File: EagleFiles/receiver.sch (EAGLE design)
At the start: 9 parts, among them IC1 MEGA8-AI

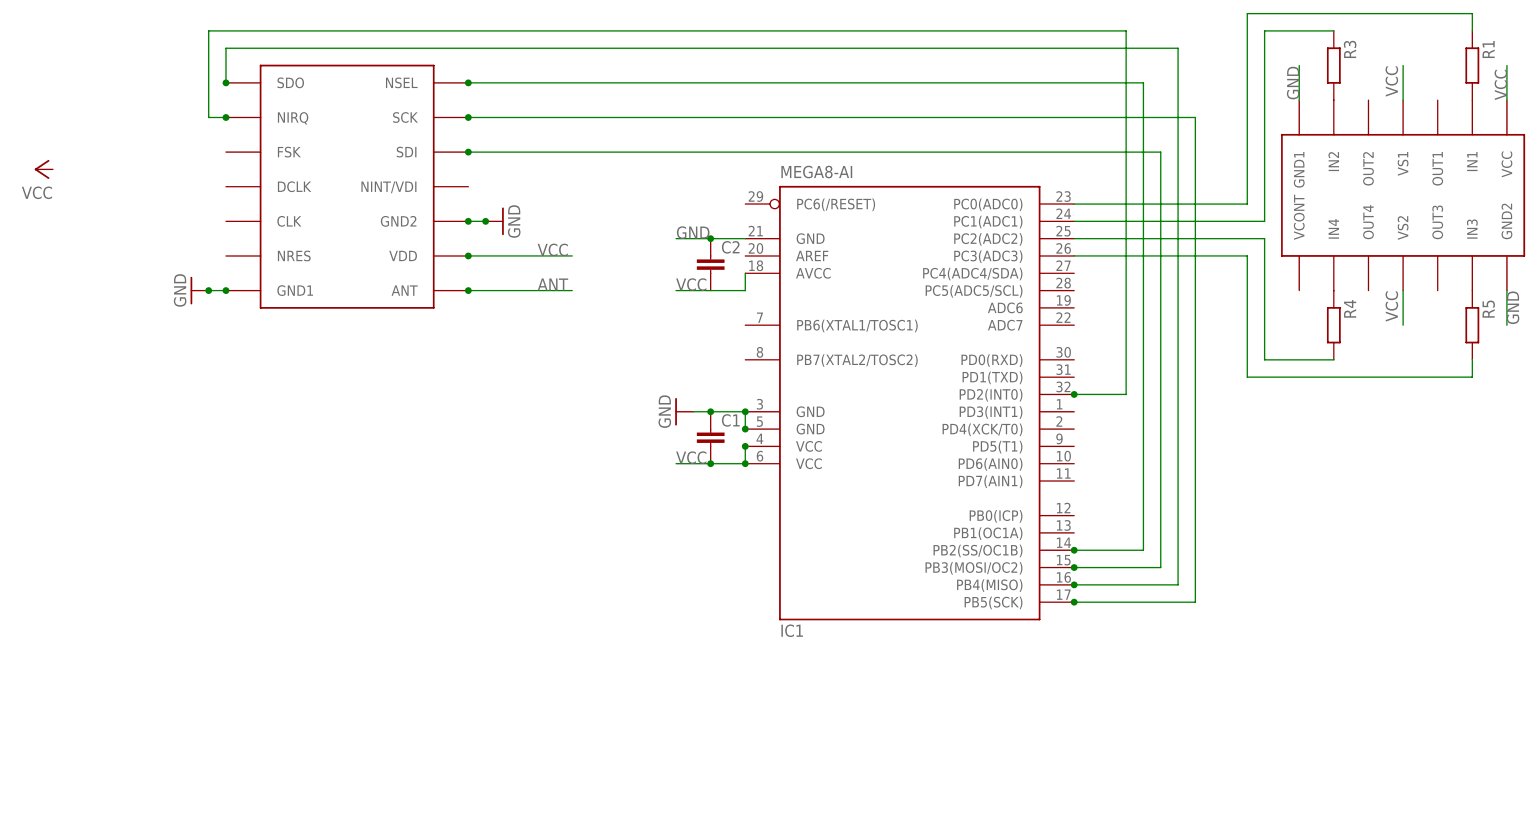
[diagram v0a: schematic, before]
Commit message: Further development of the schematic and board
Schematic finalized, added a pinheader for programming and corrected
wiring errors. Board largely designed, including pads to solder the
motor and servo wires to.
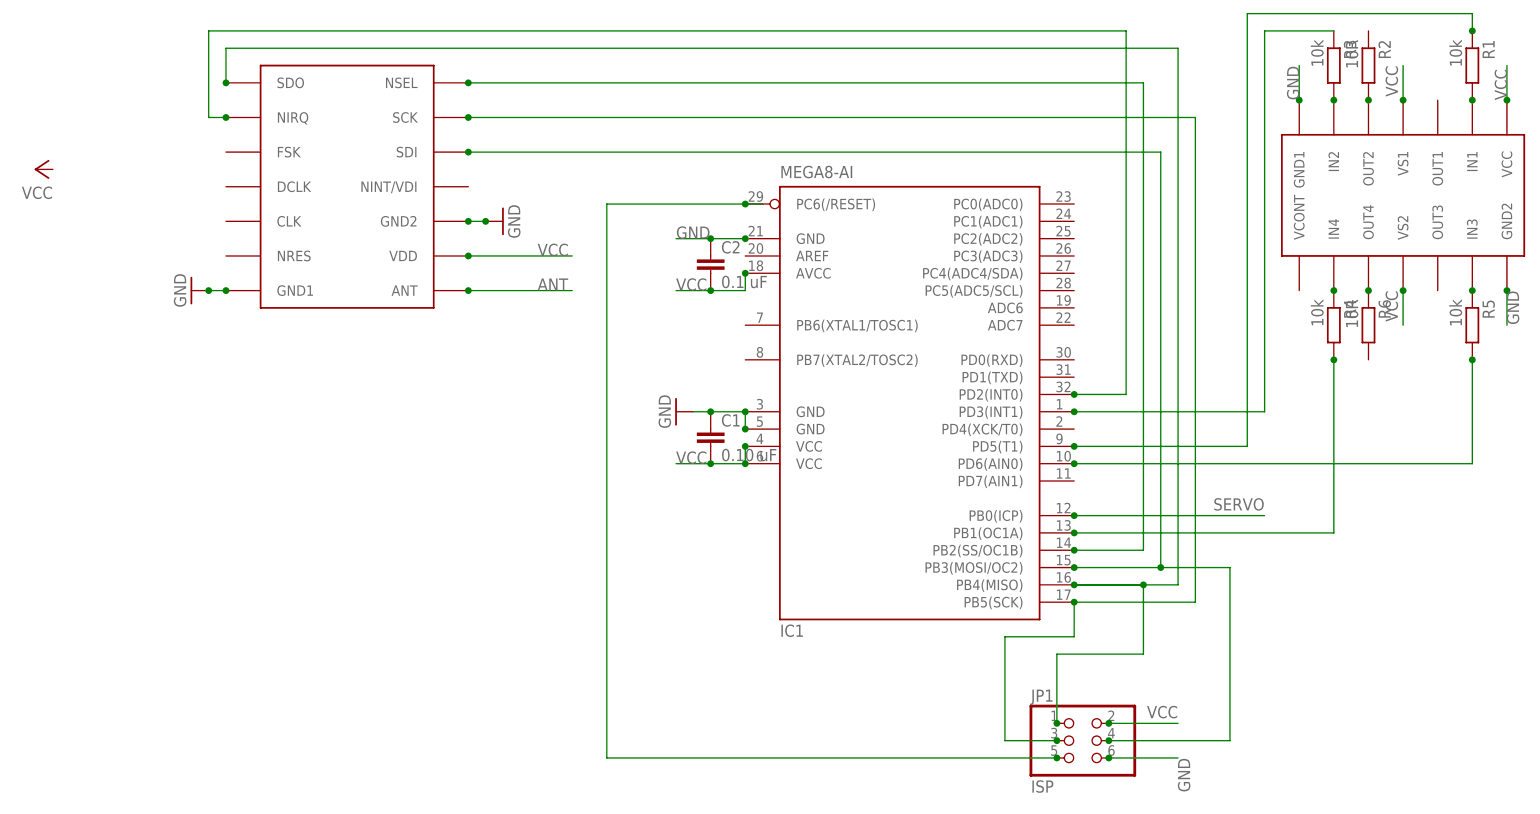
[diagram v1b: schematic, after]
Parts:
- added JP1: ISP, pinhead:PINHD-2X3
- added R2, R6: 10R, resistor:R-EU_R2012
- C1: value (none) -> 0.10 uF
- C2: value (none) -> 0.1 uF
- R1, R3, R4, R5: value (none) -> 10k
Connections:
- new net N$14: LB1836M.OUT2, R2.2
- new net N$15: LB1836M.OUT4, R6.1
- new net N$20: IC1.PC6(/RESET), JP1.5
- new net SERVO: IC1.PB0(ICP)
- net GND: now also JP1.6
- net N$1: now also JP1.1
- net N$11: now also IC1.PD3(INT1); no longer IC1.PC1(ADC1)
- net N$12: now also IC1.PB1(OC1A); no longer IC1.PC2(ADC2)
- net N$13: now also IC1.PD6(AIN0); no longer IC1.PC3(ADC3)
- net N$2: now also JP1.4
- net N$3: now also JP1.3
- net N$7: now also IC1.PD5(T1); no longer IC1.PC0(ADC0)
- net VCC: now also C2.2, JP1.2
